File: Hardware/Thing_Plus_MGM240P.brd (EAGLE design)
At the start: 22.9 x 58.4 mm, 55 parts, among them J1 THING_PLUS_LOGICAL, J2 USB Female Type C Connector, J3 QWIIC_RIGHT_ANGLE, J5 MICRO-SDFRICTION, Q1 20V/4.2A/52mΩ/1.4W, U1 MGM240P, U2 3.3V, U4 MCP73831, U5 MAX17048, U6 MK22FN128VLH10

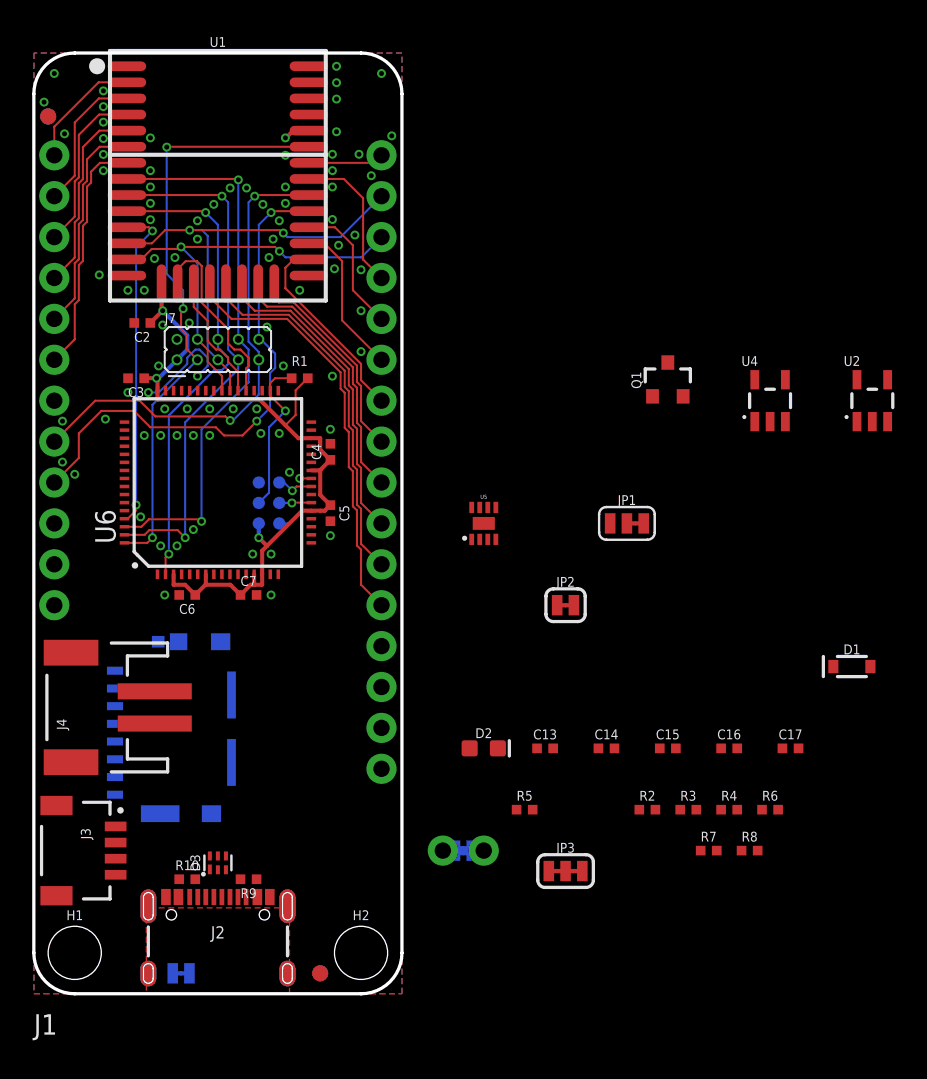
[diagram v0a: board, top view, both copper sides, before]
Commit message: Schematic and board updates
Disconnect RTS and CTS pins
Add status LED
Complete more of the routing and component placement
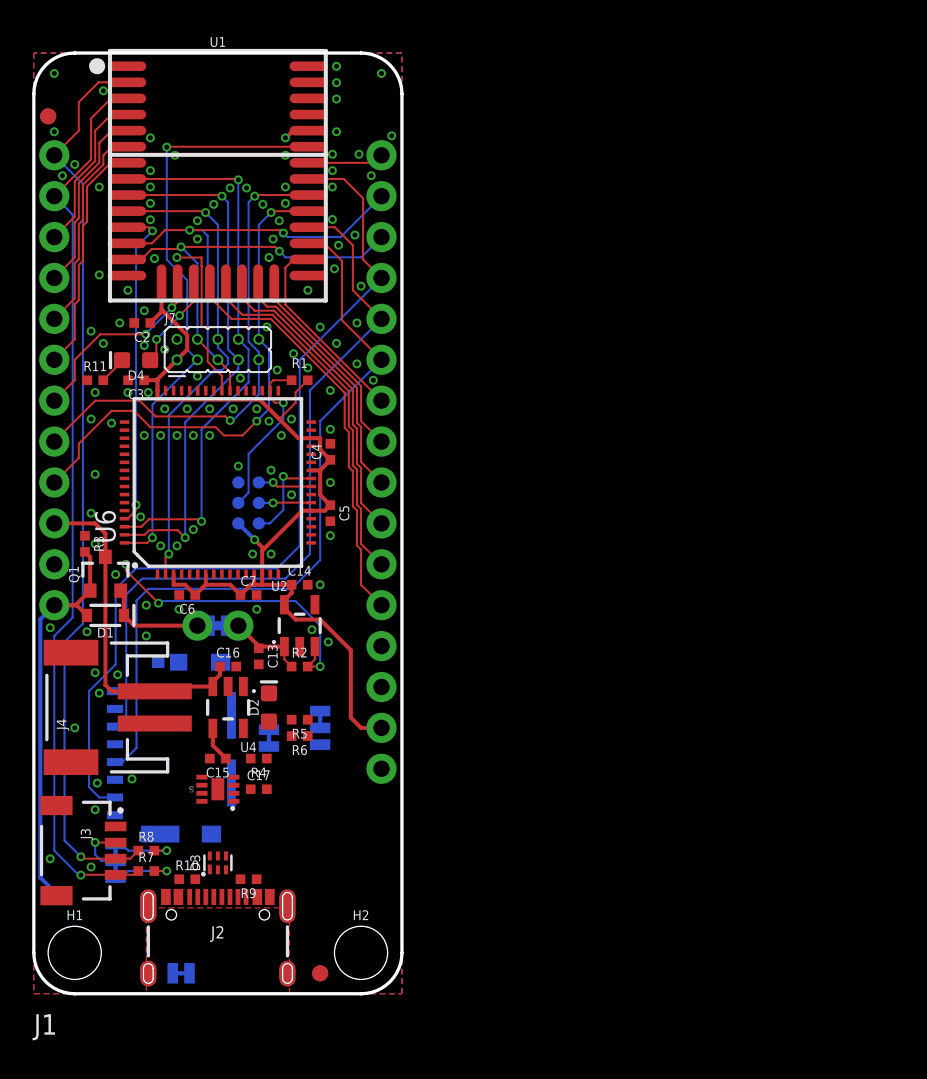
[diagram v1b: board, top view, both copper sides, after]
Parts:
- added D4: BLUE, SparkFun-LED:LED-0603
- added R11: 4.7k, SparkFun-Resistors:0402-TIGHT
- moved D1 46.5 mm to (4.45, 23.5), turned to 180 degrees
- moved R3 40.9 mm to (3.17, 27.9), turned to 270 degrees
- moved U4 38.7 mm to (12.1, 17.8), turned to 180 degrees
- moved U2 38.2 mm to (16.5, 22.9)
- moved R8 37.5 mm to (6.99, 8.89)
- moved Q1 37.0 mm to (4.45, 26.0)
- moved R7 34.9 mm to (6.99, 7.62)
- moved C17 33.1 mm to (14.0, 12.7)
- moved C16 31.5 mm to (12.1, 20.3)
- moved R6 29.6 mm to (16.5, 16.0), turned to 180 degrees
- moved R4 29.4 mm to (14.0, 14.6), turned to 180 degrees
- moved JP3 27.9 mm to (5.08, 8.26), flipped to the bottom, turned to 270 degrees
- moved C15 27.9 mm to (11.4, 14.6), turned to 180 degrees
- moved U5 23.3 mm to (11.4, 12.7), turned to 90 degrees
- moved R2 23.3 mm to (16.5, 20.3)
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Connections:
- removed net N$2: C13.1, D1.C, JP8.1, JP8.3, Q1.2, R2.1
- new net LED: D4.A, U1.17
- new net N$1: D4.C, R11.2
- new net N$7: D1.C, JP8.1, JP8.3, Q1.2
- net CTS: no longer U1.17
- net D2: now also U1.16
- net GND: now also R11.1
- net N$27: now also C13.1, R2.1
- net RTS: no longer U1.16
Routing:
- net SDA: track 7.43 -> 56.4 mm, vias 0 -> 1
- net SCL: track 8.96 -> 56.1 mm, vias 0 -> 1
- net POCI: track 9.29 -> 55.4 mm
- net PICO: track 8.50 -> 45.9 mm
- net SCK: track 9.77 -> 47.1 mm
- net V_USB: track 0.00 -> 28.1 mm
- net V_BATT: track 0.00 -> 21.2 mm
- net 3.3V: track 48.3 -> 67.0 mm, vias 3 -> 2
- net EN: track 0.00 -> 18.7 mm, vias 0 -> 3
- net D2: track 0.00 -> 12.1 mm, vias 0 -> 2
- net RTS: track 12.0 -> 0.00 mm
- net CTS: track 7.93 -> 0.00 mm
- net N$7: track 0.00 -> 6.64 mm
- net LED: track 0.00 -> 5.88 mm, vias 0 -> 2
- net N$27: track 0.00 -> 4.99 mm
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
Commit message: Finalize initial schematic and board
Clean up schematic and finalize nets
Finish routing board (needs improved GND continuity
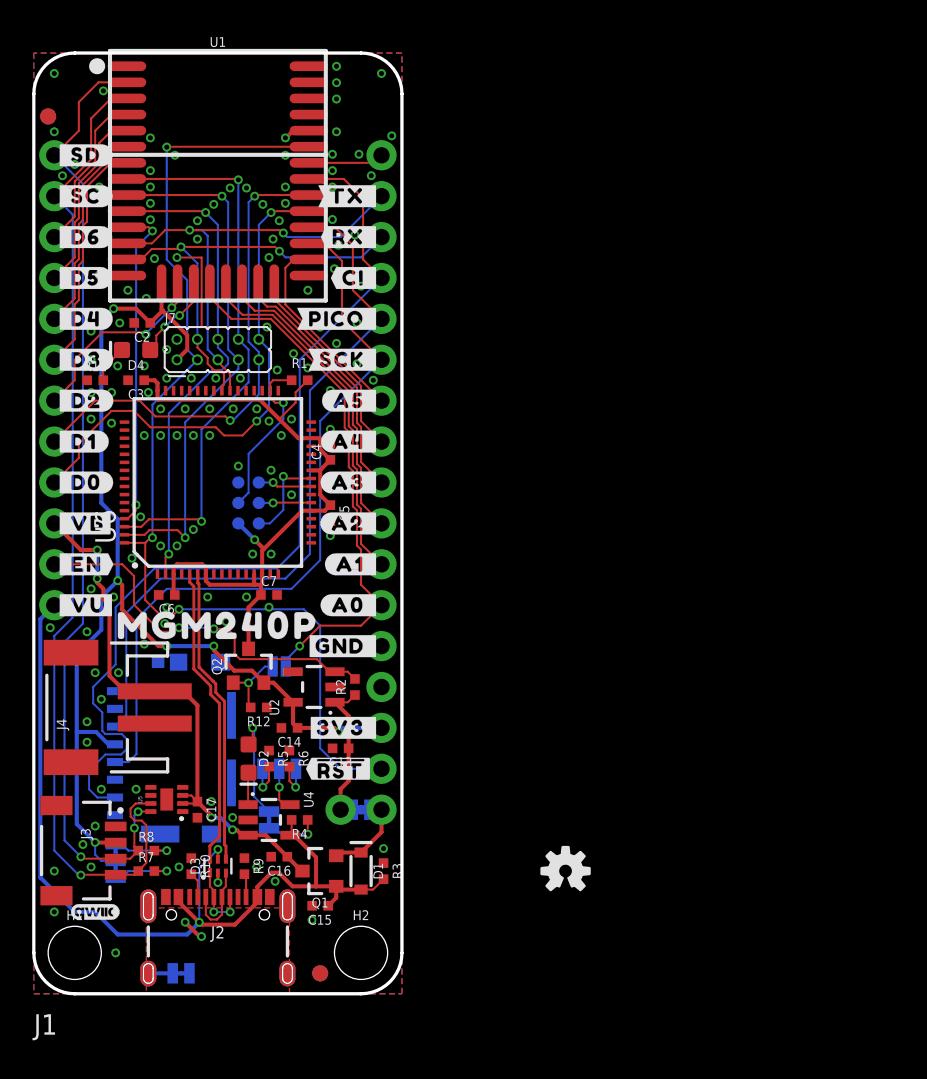
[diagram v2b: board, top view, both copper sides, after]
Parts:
- removed JP2: JUMPER-SMT_2_NC_TRACE_SILK, SparkFun-Jumpers:SMT-JUMPER_2_NC_TRACE_SILK
- removed JP8: JUMPER-COMBO_2_NC_TRACE, SparkFun-Jumpers:COMBO-JUMPER_2_NC_TRACE
- added CHG: JUMPER-SMT_2_NC_TRACE_SILK, SparkFun-Jumpers:SMT-JUMPER_2_NC_TRACE_SILK
- added LOGO1: SFE_LOGO_NAME_FLAME.1_INCH, SparkFun-Aesthetics:SFE_LOGO_NAME_FLAME_.1
- added LOGO2: QWIIC_LOGO_3MM, SparkFun-Aesthetics:QWIIC_3MM
- added LOGO3: OSHW-LOGOS, SparkFun-Aesthetics:OSHW-LOGO-S
- added MEAS: JUMPER-COMBO_2_NC_TRACE, SparkFun-Jumpers:COMBO-JUMPER_2_NC_TRACE
- added Q2: 20V/4.2A/52mΩ/1.4W, SparkFun-DiscreteSemi:SOT23-3
- added R12: 100k, SparkFun-Resistors:0402-TIGHT
- added U$1: (no value), output:#_D6#0
- added U$10: (no value), output:#_SC#0
- added U$11: (no value), output:#TX_#0
- added U$12: (no value), output:#RX_#0
- added U$13: (no value), output:#PICO_#0
- added U$14: (no value), output:#SCK_#0
- added U$15: (no value), output:#A5_#0
- added U$16: (no value), output:#A4_#0
- added U$17: (no value), output:#A3_#0
- added U$18: (no value), output:#A2_#0
- added U$19: (no value), output:#A1_#0
- added U$2: (no value), output:#_D5#0
- added U$20: (no value), output:#A0_#0
- added U$21: (no value), output:#GND_#0
- added U$22: (no value), output:#3V3_#0
- added U$23: (no value), output:MGM240P0
- added U$24: (no value), output:#CI_#0
- added U$25: (no value), output:#_VB#0
- added U$26: (no value), output:#_VU#0
- added U$27: (no value), output:#_EN#0
- added U$28: (no value), output:##RST##0
- added U$3: (no value), output:#_D4#0
- added U$4: (no value), output:#_D3#0
- added U$6: (no value), output:#_D2#0
- added U$7: (no value), output:#_D1#0
- added U$8: (no value), output:#_D0#0
- added U$9: (no value), output:#_SD#0
- added VDDJ_EN: JUMPER-SMT_2_NO_SILK, SparkFun-Jumpers:SMT-JUMPER_2_NO_SILK
- moved R3 27.5 mm to (21.7, 7.62)
- moved Q1 22.7 mm to (17.8, 7.62), turned to 90 degrees
- moved D1 22.5 mm to (20.3, 7.62), turned to 270 degrees
- moved C16 12.2 mm to (15.2, 8.51), turned to 180 degrees
- moved C15 11.1 mm to (17.8, 5.46)
- moved C14 8.91 mm to (15.9, 16.5), turned to 180 degrees
- moved C13 7.65 mm to (19.1, 15.2), turned to 180 degrees
- moved U4 7.43 mm to (14.6, 10.8), turned to 270 degrees
- moved R4 4.58 mm to (16.5, 10.8)
- moved C17 4.02 mm to (10.2, 11.4), turned to 270 degrees
- moved U2 3.91 mm to (17.4, 19.1), turned to 90 degrees
- moved R2 3.66 mm to (19.9, 19.1), turned to 90 degrees
- moved JP1 3.59 mm to (15.2, 14.0), turned to 0 degrees
- moved D2 3.42 mm to (13.3, 14.6), turned to 270 degrees
- moved U5 3.24 mm to (8.26, 12.1)
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- renumbered JP3 to I2C, JP4 to SHLD
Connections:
- removed net SCL1: U5.7
- removed net SDA1: U5.8
- new net !VDDJ_EN!: Q2.1, R12.2, VDDJ_EN.2
- new net VDD: C3.1, C4.1, C5.1, C6.1, C7.1, Q2.3, R1.2, TP1.1, U6.13, U6.14, U6.21, U6.26, U6.3, U6.30, U6.48, U6.7
- net 3.3V: now also Q2.2; no longer C3.1, C4.1, C5.1, C6.1, C7.1, R1.2, TP1.1, U6.13, U6.14, U6.21, U6.26, U6.3, U6.30, U6.48, U6.7
- net A0: now also VDDJ_EN.1
- net GND: now also R12.1
- net N$10: now also CHG.1; no longer JP2.1
- net N$27: now also MEAS.2, MEAS.4; no longer JP8.2, JP8.4
- net N$3: now also CHG.2; no longer JP2.2
- net N$7: now also MEAS.1, MEAS.3; no longer JP8.1, JP8.3
- net SCL: now also U5.7
- net SDA: now also U5.8
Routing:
- net VDD: track 0.00 -> 44.6 mm, vias 0 -> 1
- net V_USB: track 28.1 -> 57.2 mm, vias 0 -> 2
- net !RESET!: track 36.9 -> 64.2 mm, vias 2 -> 3
- net USB_P: track 0.00 -> 18.7 mm
- net USB_N: track 0.00 -> 18.4 mm
- net V_BATT: track 21.2 -> 34.1 mm, vias 0 -> 4
- net A0: track 25.8 -> 33.6 mm, vias 0 -> 1
- net N$3: track 0.00 -> 6.75 mm, vias 0 -> 1
- net SCL: track 56.1 -> 62.2 mm
- net 3.3V: track 67.0 -> 73.1 mm, vias 2 -> 6
- net N$18: track 0.00 -> 5.03 mm
- net EN: track 18.7 -> 23.5 mm, vias 3 -> 2
- net N$16: track 0.00 -> 4.50 mm, vias 0 -> 2
- net !VDDJ_EN!: track 0.00 -> 4.46 mm, vias 0 -> 1
- net N$27: track 4.99 -> 9.42 mm
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
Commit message: Add polish
Improve GND continuity
Fix and approve DRC errors
Add SFE flame and OSHW logo to top silk
Add pin and jumper labels to bottom silk
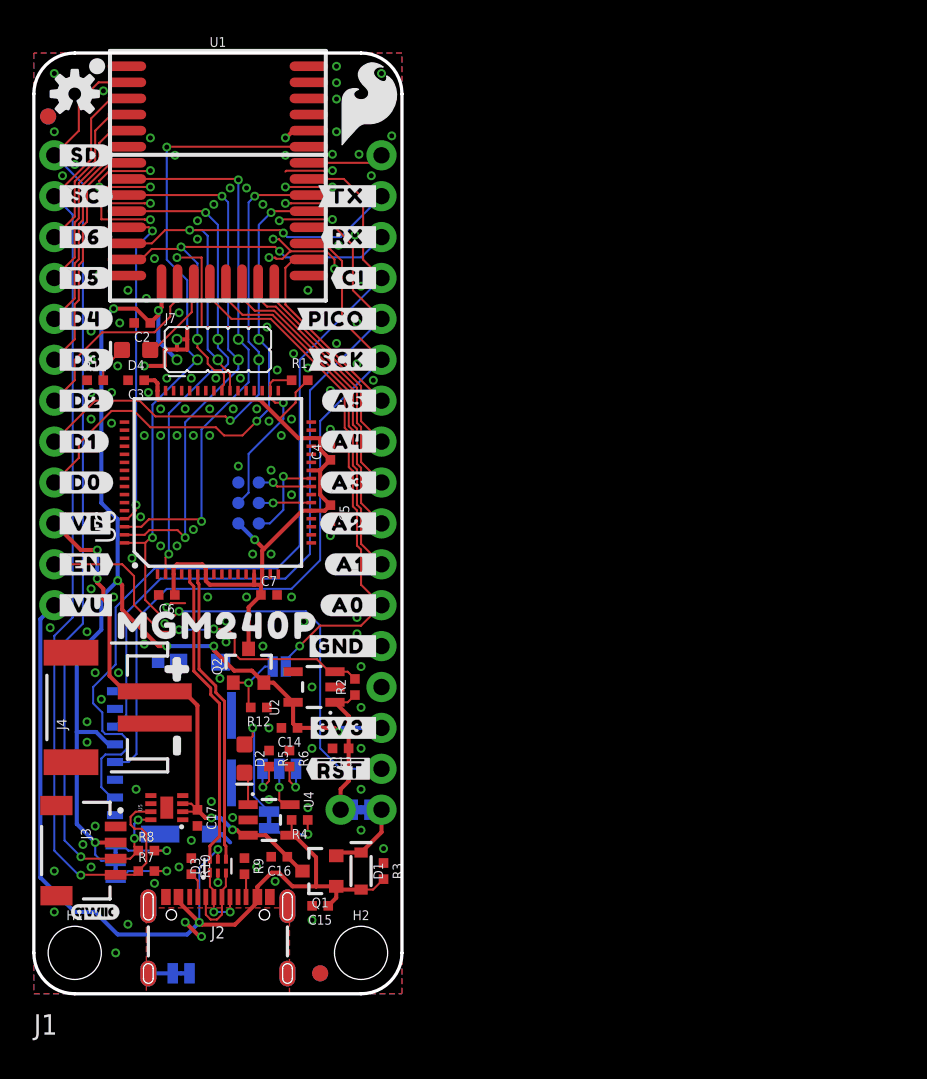
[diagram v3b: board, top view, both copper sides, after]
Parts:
- added U$29: (no value), SparkFun-Aesthetics:SFE_LOGO_FLAME_.2
- added U$30: (no value), output:#0
- added U$31: (no value), output:#1
- added U$32: (no value), output:#_PICO#0
- added U$33: (no value), output:#_POCI#0
- added U$34: (no value), output:#_RX#0
- added U$35: (no value), output:#_TX#0
- added U$36: (no value), output:#_SCK#0
- added U$37: (no value), output:#_A5#0
- added U$38: (no value), output:#_A4#0
- added U$39: (no value), output:#_A3#0
- added U$40: (no value), output:#_A2#0
- added U$41: (no value), output:#_A1#0
- added U$42: (no value), output:#_A0#0
- added U$43: (no value), output:#_GND#0
- added U$44: (no value), output:#_3V3#0
- added U$45: (no value), output:#_#RST##0
- added U$46: (no value), output:#SDA_#0
- added U$47: (no value), output:#SCL_#0
- added U$48: (no value), output:#D6_#0
- added U$49: (no value), output:#D5_#0
- added U$50: (no value), output:#D4_#0
- added U$51: (no value), output:#D3_#0
- added U$52: (no value), output:#D2_#0
- added U$53: (no value), output:#D1_#0
- added U$54: (no value), output:#D0_#0
- added U$55: (no value), output:#VBAT_#0
- added U$56: (no value), output:#VUSB_#0
- added U$57: (no value), output:#EN_#0
- added U$58: (no value), output:MGM240P0
- added U$59: (no value), output:#MEAS#0
- added U$60: (no value), output:#CHG#0
- added U$61: (no value), output:#I2C#0
- added U$62: (no value), output:#VJ_CTRL#0
- added U$63: (no value), output:#500#0
- added U$64: (no value), output:#100#0
- added U$65: (no value), output:#DBG#0
- added U$66: (no value), output:_1
- moved LOGO3 57.1 mm to (2.54, 55.9)
- moved C17 0.51 mm to (10.2, 10.9)
- moved U5 0.51 mm to (8.26, 11.6)
- moved D2 0.25 mm to (13.1, 14.6)
- moved LOGO1 0.13 mm to (11.4, 54.5)
- renumbered JP1 to CHG_I, VDDJ_EN to VJ_CTRL
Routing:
- net GND: track 13.5 -> 59.1 mm, vias 134 -> 150
- net POCI: track 57.8 -> 56.7 mm
- net SDA: track 59.8 -> 59.3 mm
- net SCL: track 62.2 -> 61.7 mm
- net 3.3V: track 73.1 -> 72.7 mm, vias 6 -> 7
- net D2: track 12.2 -> 12.3 mm, vias 2 -> 0
- net LED: track 5.36 -> 5.37 mm, vias 2 -> 0

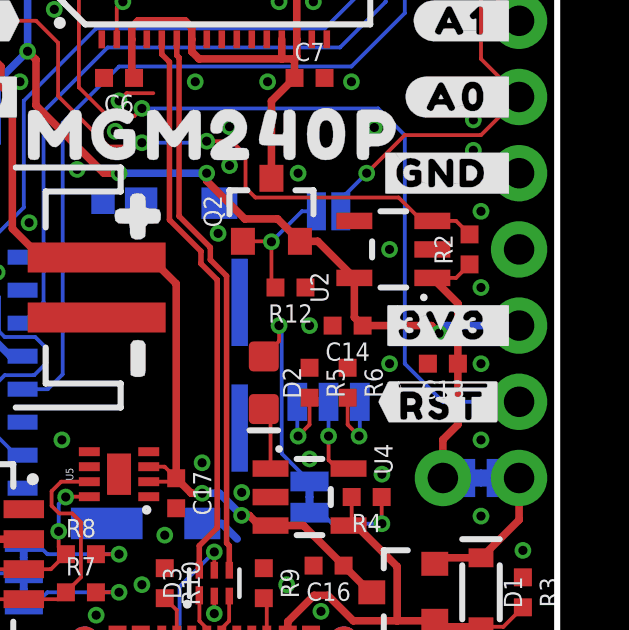
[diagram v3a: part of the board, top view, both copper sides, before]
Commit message: Update voltage regulator
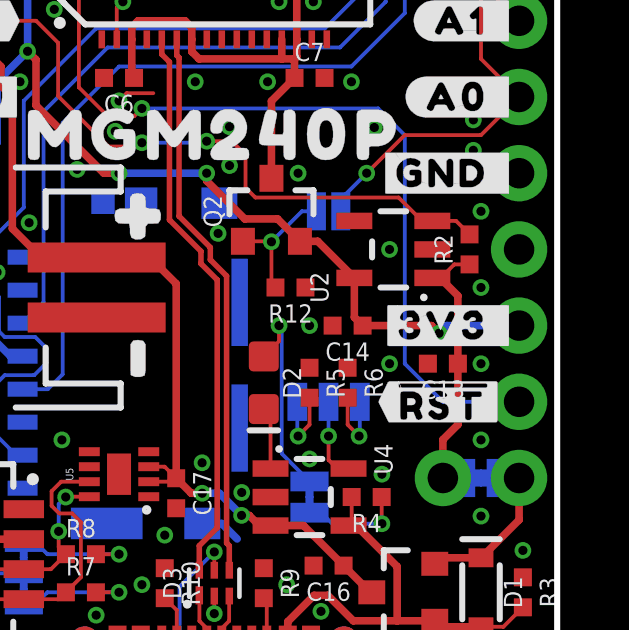
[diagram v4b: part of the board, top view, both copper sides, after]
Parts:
- U2: value 3.3V -> XC6222B331MR-G
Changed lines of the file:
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@@
 <attribute name="VALUE" x="3.175" y="16.129" size="0.6096" layer="27" font="vector" ratio="20" rot="R90"/>
 </element>
-<element name="U2" library="SparkFun-IC-Power" package="SOT23-5" value="3.3V" x="17.399" y="19.05" smashed="yes" rot="R90">
+<element name="U2" library="SparkFun-IC-Power" package="SOT23-5" value="XC6222B331MR-G" x="17.399" y="19.05" smashed="yes" rot="R90">
+<attribute name="IOUT" value="700mA" x="17.399" y="19.05" size="1.778" layer="27" rot="R90" display="off"/>
 <attribute name="NAME" x="15.24" y="17.272" size="0.6096" layer="25" ratio="20" rot="R90"/>
-<attribute name="PROD_ID" value="VREG-12457" x="7.239" y="-20.32" size="1.778" layer="27" font="vector" ratio="15" rot="R90" display="off"/>
-<attribute name="VALUE" x="20.193" y="17.272" size="0.6096" layer="27" ratio="20" rot="R90"/>
+<attribute name="PROD_ID" value="VREG-16775" x="7.239" y="-20.32" size="1.778" layer="27" font="vector" ratio="15" rot="R90" display="off"/>
+<attribute name="VOUT" value="3.3V" x="17.399" y="19.05" size="1.778" layer="27" rot="R90" display="off"/>
 </element>
 <element name="Q1" library="SparkFun-DiscreteSemi" package="SOT23-3" value="20V/4.2A/52mΩ/1.4W" x="17.78" y="7.62" smashed="yes" rot="R90">
@@
 <wire x1="19.55" y1="13.208" x2="19.55" y2="15.24" width="0.254" layer="1"/>
 <wire x1="19.55" y1="13.208" x2="19.05" y2="12.708" width="0.254" layer="1"/>
-<wire x1="19.55" y1="15.24" x2="19.55" y2="17.2491" width="0.254" layer="1"/>
-<wire x1="19.55" y1="17.2491" x2="18.6991" y2="18.1" width="0.254" layer="1"/>
-<wire x1="18.6991" y1="18.1" x2="19.489" y2="18.1" width="0.127" layer="1"/>
-<wire x1="19.489" y1="18.1" x2="19.939" y2="18.55" width="0.127" layer="1"/>
+<wire x1="19.55" y1="15.24" x2="19.55" y2="17.5031" width="0.254" layer="1"/>
+<wire x1="19.55" y1="17.5031" x2="18.9531" y2="18.1" width="0.254" layer="1"/>
+<wire x1="18.9531" y1="18.1" x2="18.6991" y2="18.1" width="0.254" layer="1"/>
+<wire x1="18.6991" y1="18.1" x2="18.981" y2="18.1" width="0.127" layer="1"/>
+<wire x1="19.431" y1="18.55" x2="19.939" y2="18.55" width="0.127" layer="1"/>
+<wire x1="19.431" y1="18.55" x2="18.981" y2="18.1" width="0.127" layer="1"/>
 <wire x1="19.05" y1="11.43" x2="19.812" y2="11.43" width="0.254" layer="16"/>
 </signal>
